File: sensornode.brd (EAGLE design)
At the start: 112.3 x 61 mm, 76 parts, among them IC1 CP2104, Q1 mmbt2222, Q2 mmbt2222, Q3 DMG3415U, SW2 KMR2, U1 TSL2591, U2 AP2112-3.3, U3 MCP73831T-2ACI/OT, U4 BMEx80, X2 ESP32_WROOM32_SKINNY, X4 20329

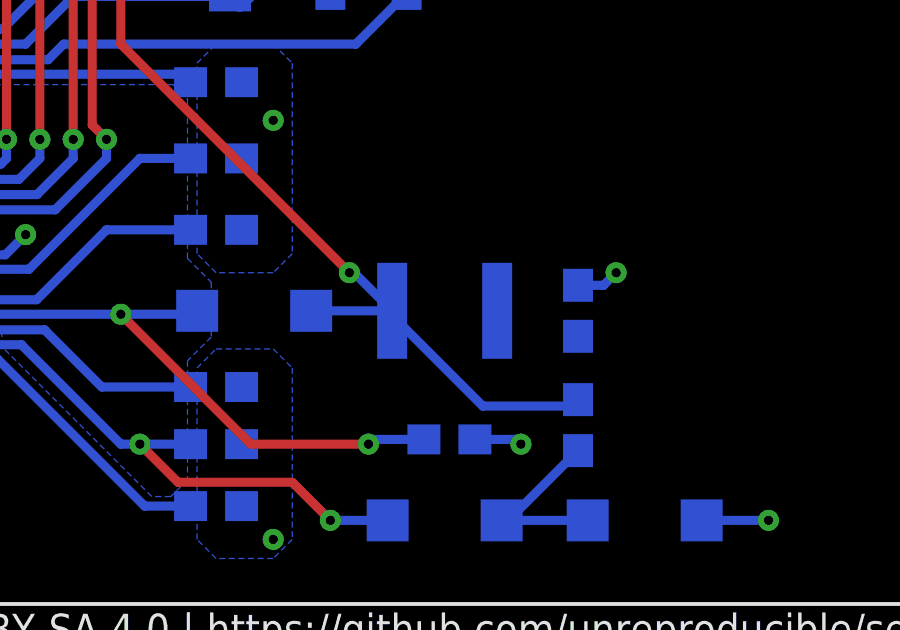
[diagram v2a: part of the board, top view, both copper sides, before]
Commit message: Modifications to fix the e-ink screen drivers
So turns out the e-ink screen needs two fixes:
1) The inductor pad is just straight up wrong, so I've replaced that
1.1) I've also moved from a 68uH coil to a 10uH1A coil (matching Good
  Display's DESPI-C02 more closely)
2) The R16 resistor should not, in fact, be 2.2Ohm, it should be 0.47Ohm
	(though I'll note 1Ohm works)

I believe at this point this is now a garaunteed fully working circuit.
Any additional changes would just need to replicate what the DESPI-C02
does, but the original design on the sensornode works with if you swap
the R16 resistor.
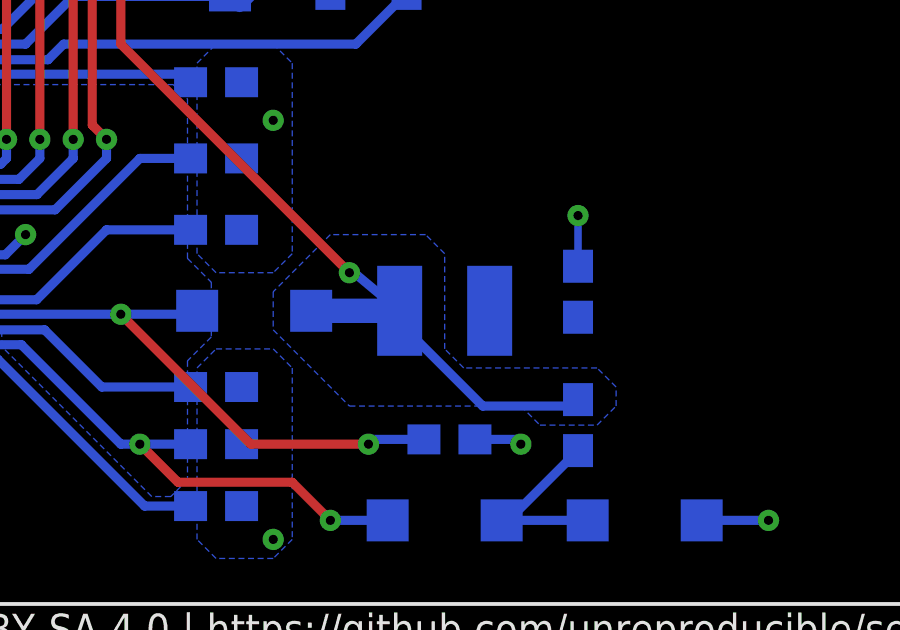
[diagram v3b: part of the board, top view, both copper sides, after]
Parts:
- L1: value INDUCTOR-1812-68uH-220ma -> 10uH1A - 1812; device SparkFun-Coils:1812 -> John - Inductors:1815
- R16: value 2.2 -> 0.47
- moved C13 0.63 mm to (61.6, 12.1)
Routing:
- net N$14: track 27.1 -> 27.7 mm
- added copper zone on layer 16, net N$14
